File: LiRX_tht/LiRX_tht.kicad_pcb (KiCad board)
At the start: 2 copper layers, 60 x 30 mm, 38 parts, among them J1 TP8, J10 onoff, J11 TP9, J2 TP3, J3 TP4, J4 buchse, J5 TP2, J6 TP5, J7 TP7, J8 TP1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

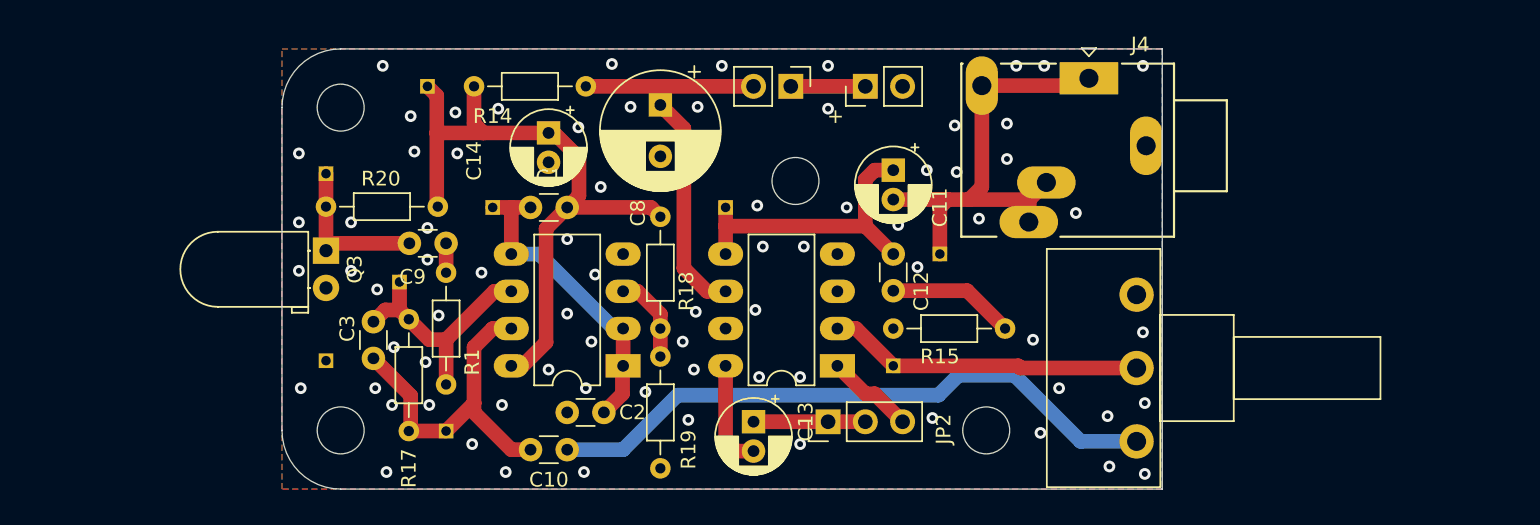
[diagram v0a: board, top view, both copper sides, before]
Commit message: Added Suggestions; 1cm longer; kicad 6.0
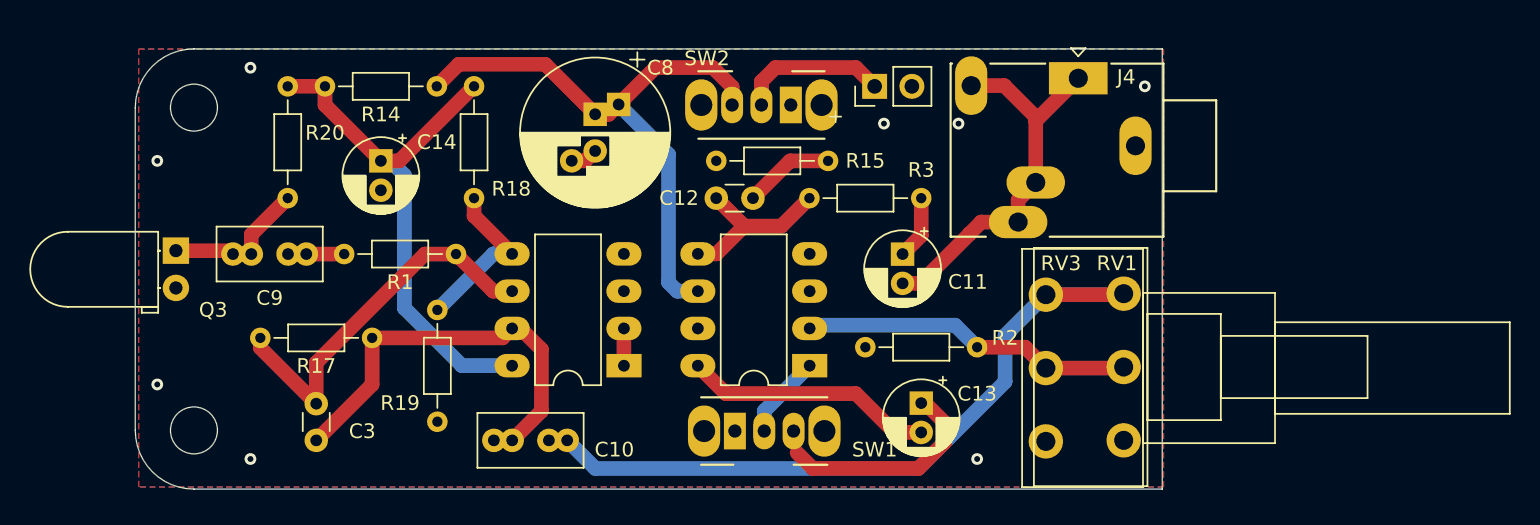
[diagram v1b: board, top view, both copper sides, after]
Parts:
- removed C1, C2: 100n, Capacitor_THT:C_Disc_D3.0mm_W1.6mm_P2.50mm
- removed H3, H4: MountingHole, MountingHole:MountingHole_3.2mm_M3
- removed J1: TP8, Connector_PinHeader_1.27mm:PinHeader_1x01_P1.27mm_Vertical
- removed J10: onoff, Connector_PinHeader_2.54mm:PinHeader_1x02_P2.54mm_Vertical
- removed J11: TP9, Connector_PinHeader_1.27mm:PinHeader_1x01_P1.27mm_Vertical
- removed J2: TP3, Connector_PinHeader_1.27mm:PinHeader_1x01_P1.27mm_Vertical
- removed J3: TP4, Connector_PinHeader_1.27mm:PinHeader_1x01_P1.27mm_Vertical
- removed J5: TP2, Connector_PinHeader_1.27mm:PinHeader_1x01_P1.27mm_Vertical
- removed J6: TP5, Connector_PinHeader_1.27mm:PinHeader_1x01_P1.27mm_Vertical
- removed J7: TP7, Connector_PinHeader_1.27mm:PinHeader_1x01_P1.27mm_Vertical
- removed J8: TP1, Connector_PinHeader_1.27mm:PinHeader_1x01_P1.27mm_Vertical
- removed J9: TP6, Connector_PinHeader_1.27mm:PinHeader_1x01_P1.27mm_Vertical
- removed JP2: gain, Connector_PinHeader_2.54mm:PinHeader_1x03_P2.54mm_Vertical
- added R2: 680, Resistor_THT:R_Axial_DIN0204_L3.6mm_D1.6mm_P7.62mm_Horizontal, F.Cu at (119.4, 100.3)
- added R3: 270, Resistor_THT:R_Axial_DIN0204_L3.6mm_D1.6mm_P7.62mm_Horizontal, F.Cu at (108.0, 90.2)
- added RV1: 10k, Potentiometer_THT:Potentiometer_Piher_T-16H_Single_Horizontal, F.Cu at (129.4, 106.7)
- added SW1: gain, Button_Switch_THT:SW_CuK_OS102011MA1QN1_SPDT_Angled, F.Cu at (102.9, 106.0)
- added SW2: onoff, Button_Switch_THT:SW_CuK_OS102011MA1QN1_SPDT_Angled, F.Cu at (106.7, 83.8)
- C10, C9: footprint Capacitor_THT:C_Disc_D3.0mm_W1.6mm_P2.50mm -> Capacitor_THT:C_Rect_L7.0mm_W3.5mm_P2.50mm_P5.00mm
- C8: footprint Capacitor_THT:CP_Radial_D8.0mm_P3.50mm -> Capacitor_THT:CP_Radial_D10.0mm_P2.50mm_P5.00mm
- R18, R19: value 1M -> 12k
- RV3: footprint Potentiometer_THT:Potentiometer_Piher_T-16H_Single_Horizontal -> Potentiometer_THT:Potentiometer_Piher_PC-16_Single_Horizontal
- moved R15 16.6 mm to (101.6, 87.6)
- moved R19 15.5 mm to (82.6, 97.8)
- moved R18 15.5 mm to (85.1, 82.5)
- moved R20 13.1 mm to (72.4, 82.5), turned to -90 degrees
- moved C12 12.7 mm to (101.6, 90.2), turned to 0 degrees
- moved C14 11.6 mm to (78.7, 87.6)
- moved C13 11.5 mm to (115.6, 104.1)
- moved Q3 10.2 mm to (64.8, 93.8)
- moved R14 10.2 mm to (82.5, 82.5)
- moved H1 10.0 mm to (66.0, 84.0)
- moved H2 10.0 mm to (66.0, 106.0)
- moved C9 9.55 mm to (73.7, 94.0)
- moved R1 8.92 mm to (83.9, 94.0), turned to 180 degrees
- moved R17 6.82 mm to (78.1, 99.7), turned to 180 degrees
- moved C3 6.81 mm to (74.3, 106.7)
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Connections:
- net TP7 renamed Net-(R2-Pad1)
- net TP9 renamed Net-(C11-Pad2)
- net VEE renamed Net-(C8-Pad1)
- C11 pad 1: TP8 -> Net-(C11-Pad1)
- C12 pad 1: TP8 -> Net-(C12-Pad1)
- RV3 pad 1: Net-(C10-Pad1) -> GND
- RV3 pad 3: GND -> Net-(C10-Pad1)
- U2 pad 5: TP8 -> Net-(C12-Pad1)
- U2 pad 7: (no net) -> unconnected-(U2-Pad7)
- U3 pad 1: TP3 -> Net-(U3-Pad1)
- U3 pad 2: TP3 -> Net-(U3-Pad1)
- U3 pad 3: Net-(R18-Pad2) -> GND
- U3 pad 5: TP3 -> Net-(R18-Pad2)
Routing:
- net TP3: track 21.7 -> 0.00 mm
- net TP8: track 20.7 -> 0.00 mm
- net Net-(C8-Pad1): track 28.0 -> 41.0 mm
- net Net-(C12-Pad1): track 0.00 -> 11.9 mm
- net Net-(C13-Pad2): track 7.29 -> 17.1 mm
- net TP5: track 16.9 -> 26.3 mm
- net Net-(C10-Pad1): track 42.8 -> 52.1 mm
- net TP2: track 45.5 -> 37.7 mm
- net Net-(C13-Pad1): track 7.62 -> 14.7 mm
- net Net-(C11-Pad2): track 32.7 -> 26.7 mm
- net TP6: track 23.7 -> 29.2 mm
- net Net-(R18-Pad2): track 6.08 -> 11.6 mm
- net Net-(C11-Pad1): track 0.00 -> 4.34 mm
- net Net-(U3-Pad1): track 0.00 -> 2.54 mm
- net Net-(C12-Pad2): track 8.69 -> 6.17 mm
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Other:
- board size 60 x 30 mm -> 70 x 30 mm
- net class Default removed
- net class thick removed
- board text added: "LiRX"
